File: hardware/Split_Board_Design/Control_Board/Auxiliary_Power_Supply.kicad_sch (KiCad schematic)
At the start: 25 parts, among them U7 TLV1117-33, U8 LV14340DDAR

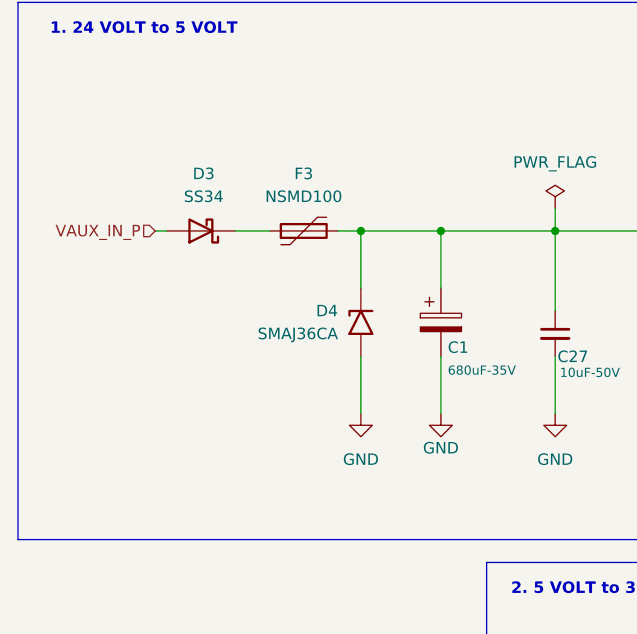
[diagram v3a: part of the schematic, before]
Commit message: feat(layout): update control board layout
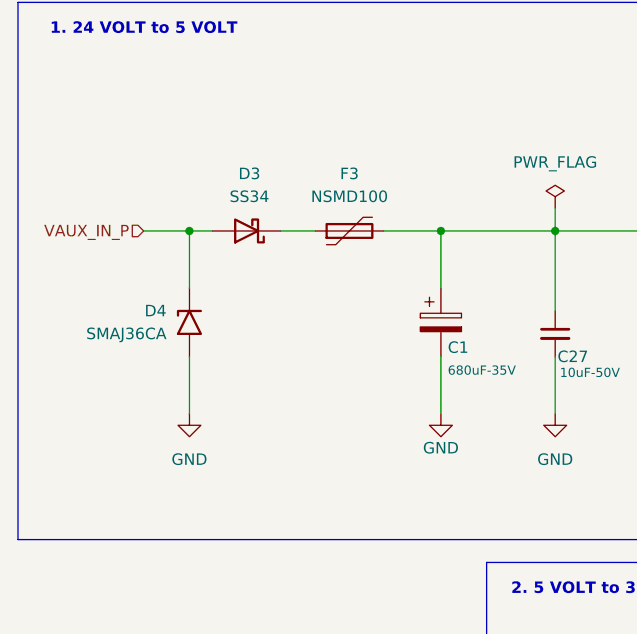
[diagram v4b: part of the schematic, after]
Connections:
- net +24V: no longer D4.1 (A1)
- net VAUX_IN_P: now also D4.1 (A1)
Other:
- moved on the sheet: D3, D4, F3
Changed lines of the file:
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@@
 	)
 	(junction
-		(at 62.23 58.42)
-		(diameter 0)
-		(color 0 0 0 0)
-	)
-	(junction
 		(at 100.33 58.42)
 		(diameter 0)
@@
 	)
 	(junction
-		(at 134.62 114.3)
+		(at 34.29 58.42)
 		(diameter 0)
 		(color 0 0 0 0)
 	)
 	(junction
-		(at 180.34 41.91)
+		(at 134.62 114.3)
 		(diameter 0)
 		(color 0 0 0 0)
 	)
 	(junction
-		(at 74.93 58.42)
+		(at 180.34 41.91)
 		(diameter 0)
 		(color 0 0 0 0)
 	)
 	(junction
-		(at 53.34 58.42)
+		(at 74.93 58.42)
 		(diameter 0)
 		(color 0 0 0 0)
@@
 	)
 	(junction
+		(at 62.23 58.42)
+		(diameter 0)
+		(color 0 0 0 0)
+	)
+	(junction
 		(at 180.34 58.42)
 		(diameter 0)
@@
 	(wire
 		(pts
+			(xy 34.29 58.42) (xy 34.29 64.77)
+		)
+		(stroke
+			(width 0)
+			(type default)
+		)
+	)
+	(wire
+		(pts
 			(xy 179.07 76.2) (xy 179.07 73.66)
 		)
@@
 	(wire
 		(pts
-			(xy 53.34 58.42) (xy 62.23 58.42)
+			(xy 55.88 58.42) (xy 62.23 58.42)
 		)
 		(stroke
@@
 	(wire
 		(pts
-			(xy 53.34 58.42) (xy 53.34 64.77)
-		)
-		(stroke
-			(width 0)
-			(type default)
-		)
-	)
-	(wire
-		(pts
-			(xy 53.34 72.39) (xy 53.34 78.74)
+			(xy 34.29 72.39) (xy 34.29 78.74)
 		)
 		(stroke
@@
 	(wire
 		(pts
-			(xy 31.75 58.42) (xy 30.48 58.42)
+			(xy 36.83 58.42) (xy 34.29 58.42)
 		)
 		(stroke
@@
 	(wire
 		(pts
-			(xy 50.8 58.42) (xy 53.34 58.42)
-		)
-		(stroke
-			(width 0)
-			(type default)
-		)
-	)
-	(wire
-		(pts
 			(xy 114.3 41.91) (xy 114.3 55.88)
 		)
@@
 	(wire
 		(pts
-			(xy 39.37 58.42) (xy 43.18 58.42)
+			(xy 44.45 58.42) (xy 48.26 58.42)
 		)
 		(stroke
@@
 	(wire
 		(pts
+			(xy 34.29 58.42) (xy 29.21 58.42)
+		)
+		(stroke
+			(width 0)
+			(type default)
+		)
+	)
+	(wire
+		(pts
 			(xy 194.31 46.99) (xy 194.31 41.91)
 		)
@@
 	(hierarchical_label "VAUX_IN_P"
 		(shape input)
-		(at 30.48 58.42 180)
+		(at 29.21 58.42 180)
 		(effects
 			(font
@@
 	(symbol
 		(lib_id "Device:Polyfuse")
-		(at 46.99 58.42 90)
+		(at 52.07 58.42 90)
 		(unit 1)
 		(body_style 1)
@@
 		(fields_autoplaced yes)
 		(property "Reference" "F3"
-			(at 46.99 52.07 90)
+			(at 52.07 52.07 90)
 			(show_name no)
 			(do_not_autoplace no)
@@
 		)
 		(property "Value" "NSMD100"
-			(at 46.99 54.61 90)
+			(at 52.07 54.61 90)
 			(show_name no)
 			(do_not_autoplace no)
@@
 		)
 		(property "Footprint" "Fuse:Fuse_1206_3216Metric"
-			(at 52.07 57.15 0)
+			(at 57.15 57.15 0)
 			(hide yes)
 			(show_name no)
@@
 		)
 		(property "Datasheet" "https://www.lcsc.com/datasheet/C66453.pdf"
-			(at 46.99 58.42 0)
+			(at 52.07 58.42 0)
 			(hide yes)
 			(show_name no)
@@
 		)
 		(property "Description" "Fuse 1A"
-			(at 46.99 58.42 0)
+			(at 52.07 58.42 0)
 			(hide yes)
 			(show_name no)
@@
 		)
 		(property "Link to Buy" "https://linhkienthuduc.com/san-pham/nsmd100-cau-chi-tu-phuc-hoi-60v-1a-1206/"
-			(at -22.86 0 0)
+			(at -17.78 0 0)
 			(hide yes)
 			(show_name no)
@@
 		)
 		(property "MPN" "nSMD100"
-			(at -22.86 0 0)
+			(at -17.78 0 0)
 			(hide yes)
 			(show_name no)
@@
 		)
 		(property "LCSC Part" "C66453"
-			(at -22.86 0 0)
+			(at -17.78 0 0)
 			(hide yes)
 			(show_name no)
@@
 		)
 		(property "BOM Comments" ""
-			(at 46.99 58.42 90)
+			(at 52.07 58.42 90)
 			(hide yes)
 			(show_name no)
@@
 		)
 		(property "DigiKey_Part_Number" ""
-			(at 46.99 58.42 90)
+			(at 52.07 58.42 90)
 			(hide yes)
 			(show_name no)
@@
 		)
 		(property "Link" ""
-			(at 46.99 58.42 90)
+			(at 52.07 58.42 90)
 			(hide yes)
 			(show_name no)
@@
 		)
 		(property "Sim.Type" ""
-			(at 46.99 58.42 90)
+			(at 52.07 58.42 90)
 			(hide yes)
 			(show_name no)
@@
 		)
 		(property "VENDOR" ""
-			(at 46.99 58.42 90)
+			(at 52.07 58.42 90)
 			(hide yes)
 			(show_name no)
@@
 		)
 		(property "CREATOR" ""
-			(at 46.99 58.42 90)
+			(at 52.07 58.42 90)
 			(hide yes)
 			(show_name no)
@@
 	(symbol
 		(lib_id "power:GND")
-		(at 53.34 78.74 0)
+		(at 34.29 78.74 0)
 		(unit 1)
 		(body_style 1)
@@
 		(fields_autoplaced yes)
 		(property "Reference" "#PWR065"
-			(at 53.34 85.09 0)
+			(at 34.29 85.09 0)
 			(hide yes)
 			(show_name no)
@@
 		)
 		(property "Value" "GND"
-			(at 53.34 83.82 0)
+			(at 34.29 83.82 0)
 			(show_name no)
 			(do_not_autoplace no)
@@
 		)
 		(property "Footprint" ""
-			(at 53.34 78.74 0)
+			(at 34.29 78.74 0)
 			(hide yes)
 			(show_name no)
@@
 		)
 		(property "Datasheet" ""
-			(at 53.34 78.74 0)
+			(at 34.29 78.74 0)
 			(hide yes)
 			(show_name no)
@@
 		)
 		(property "Description" "Power symbol creates a global label with name \"GND\" , ground"
-			(at 53.34 78.74 0)
+			(at 34.29 78.74 0)
 			(hide yes)
 			(show_name no)
@@
 	(symbol
 		(lib_id "Diode:SS34")
-		(at 35.56 58.42 180)
+		(at 40.64 58.42 180)
 		(unit 1)
 		(body_style 1)
@@
 		(fields_autoplaced yes)
 		(property "Reference" "D3"
-			(at 35.8775 52.07 0)
+			(at 40.9575 52.07 0)
 			(show_name no)
 			(do_not_autoplace no)
@@
 		)
 		(property "Value" "SS34"
-			(at 35.8775 54.61 0)
+			(at 40.9575 54.61 0)
 			(show_name no)
 			(do_not_autoplace no)
@@
 		)
 		(property "Footprint" "Diode_SMD:D_SMA"
-			(at 35.56 53.975 0)
+			(at 40.64 53.975 0)
 			(hide yes)
 			(show_name no)
@@
 		)
 		(property "Datasheet" "https://www.vishay.com/docs/88751/ss32.pdf"
-			(at 35.56 58.42 0)
+			(at 40.64 58.42 0)
 			(hide yes)
 			(show_name no)
@@
 		)
 		(property "Description" "40V 3A Schottky Diode, SMA"
-			(at 35.56 58.42 0)
+			(at 40.64 58.42 0)
 			(hide yes)
 			(show_name no)
@@
 		)
 		(property "Link to Buy" "https://linhkien.cxtvn.com/1128-diode-ss34-sma-3a-40v-do-214ac.html"
-			(at -20.32 0 0)
+			(at -15.24 0 0)
 			(hide yes)
 			(show_name no)
@@
 		)
 		(property "LCSC Part" "C2837271"
-			(at -20.32 0 0)
+			(at -15.24 0 0)
 			(hide yes)
 			(show_name no)
@@
 		)
 		(property "BOM Comments" ""
-			(at 35.56 58.42 0)
+			(at 40.64 58.42 0)
 			(hide yes)
 			(show_name no)
@@
 		)
 		(property "DigiKey_Part_Number" ""
-			(at 35.56 58.42 0)
+			(at 40.64 58.42 0)
 			(hide yes)
 			(show_name no)
@@
 		)
 		(property "Link" ""
-			(at 35.56 58.42 0)
+			(at 40.64 58.42 0)
 			(hide yes)
 			(show_name no)
@@
 		)
 		(property "Sim.Type" ""
-			(at 35.56 58.42 0)
+			(at 40.64 58.42 0)
 			(hide yes)
 			(show_name no)
@@
 		)
 		(property "VENDOR" ""
-			(at 35.56 58.42 0)
+			(at 40.64 58.42 0)
 			(hide yes)
 			(show_name no)
@@
 		)
 		(property "CREATOR" ""
-			(at 35.56 58.42 0)
+			(at 40.64 58.42 0)
 			(hide yes)
 			(show_name no)
@@
 	(symbol
 		(lib_id "Diode:SMAJ36A")
-		(at 53.34 68.58 90)
+		(at 34.29 68.58 90)
 		(mirror x)
 		(unit 1)
@@
 		(dnp no)
 		(property "Reference" "D4"
-			(at 50.8 67.3099 90)
+			(at 31.75 67.3099 90)
 			(show_name no)
 			(do_not_autoplace no)
@@
 		)
 		(property "Value" "SMAJ36CA"
-			(at 50.8 69.8499 90)
+			(at 31.75 69.8499 90)
 			(show_name no)
 			(do_not_autoplace no)
@@
 		)
 		(property "Footprint" "Diode_SMD:D_SMA"
-			(at 58.42 68.58 0)
+			(at 39.37 68.58 0)
 			(hide yes)
 			(show_name no)
@@
 		)
 		(property "Datasheet" "https://www.littelfuse.com/media?resourcetype=datasheets&itemid=75e32973-b177-4ee3-a0ff-cedaf1abdb93&filename=smaj-datasheet"
-			(at 53.34 67.31 0)
+			(at 34.29 67.31 0)
 			(hide yes)
 			(show_name no)
@@
 		)
 		(property "Description" "400W unidirectional Transient Voltage Suppressor, 36.0Vr, SMA(DO-214AC)"
-			(at 53.34 68.58 0)
+			(at 34.29 68.58 0)
 			(hide yes)
 			(show_name no)
@@
 		)
 		(property "Link to Buy" "https://linhkienthuduc.com/san-pham/smaj36ca-tvs-diodes-400w-36v/"
-			(at 2.54 0 0)
+			(at -16.51 0 0)
 			(hide yes)
 			(show_name no)
@@
 		)
 		(property "LCSC Part" "C113967"
-			(at 2.54 0 0)
+			(at -16.51 0 0)
 			(hide yes)
 			(show_name no)
@@
 		)
 		(property "BOM Comments" ""
-			(at 53.34 68.58 90)
+			(at 34.29 68.58 90)
 			(hide yes)
 			(show_name no)
@@
 		)
 		(property "DigiKey_Part_Number" ""
-			(at 53.34 68.58 90)
+			(at 34.29 68.58 90)
 			(hide yes)
 			(show_name no)
@@
 		)
 		(property "Link" ""
-			(at 53.34 68.58 90)
+			(at 34.29 68.58 90)
 			(hide yes)
 			(show_name no)
@@
 		)
 		(property "Sim.Type" ""
-			(at 53.34 68.58 90)
+			(at 34.29 68.58 90)
 			(hide yes)
 			(show_name no)
@@
 		)
 		(property "VENDOR" ""
-			(at 53.34 68.58 90)
+			(at 34.29 68.58 90)
 			(hide yes)
 			(show_name no)
@@
 		)
 		(property "CREATOR" ""
-			(at 53.34 68.58 90)
+			(at 34.29 68.58 90)
 			(hide yes)
 			(show_name no)

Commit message: layout: update layout
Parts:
- removed C28: 10uF-50V, Capacitor_SMD:C_0603_1608Metric, symbol Device:C_Small
- removed D4: SMAJ36CA, Diode_SMD:D_SMA, symbol Diode:SMAJ36A
- added D4: SMAJ24A, Diode_SMD:D_SMA, symbol Diode:SMAJ24A
- C1: value 680uF-35V -> 100uF-50V; footprint RobotChargeController:CP_Elec_12.5x13.5_Generic_H13 -> Capacitor_SMD:CP_Elec_8x10.5; Link to Buy https://linhkien.cxtvn.com/3037-tu-nhom-680uf-35v-125x135mm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 -> https://linhkien.cxtvn.com/3033-tu-nhom-100uf-50v-8x105-5c.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
- R10: value 49.9R -> 49.9kR; Link to Buy https://linhkienthuduc.com/san-pham/dien-tro-49-9-ohm-0603-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 -> (none); MPN 49R9 0603 1% -> (none)
- U8: footprint SOIC8_DDA_TEX -> RobotChargeController:SOIC8_DDA_TEX
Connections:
- net +24V: now also D3.1 (K); no longer F3.2
- net GND: now also D4.2 (A2)
- net VAUX_IN_P: now also F3.1; no longer D3.2 (A)
- new net: D3.2 (A), D4.1 (A1), F3.2
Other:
- moved on the sheet: C42, D3
